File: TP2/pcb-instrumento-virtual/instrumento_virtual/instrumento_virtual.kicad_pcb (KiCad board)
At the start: 2 copper layers, 90 parts, among them J1 Conn_01x09_Pin, J2 Conector_salidas_analógicas, J3 Conn_01x20_Socket, J4 Conn_01x09_Pin, J5 Conn_01x20_Socket, J7 RS232, Q10 BC547, Q3 BC547, Q4 BC547, Q5 BC547, Q6 BC547, Q7 BC547, Q8 BC547, Q9 BC547, U1 CD4051B, U2 MCP6002-xMC, U4 AMS1117-3.3, U5 AMS1117-5.0, U6 MCP6002-xMC

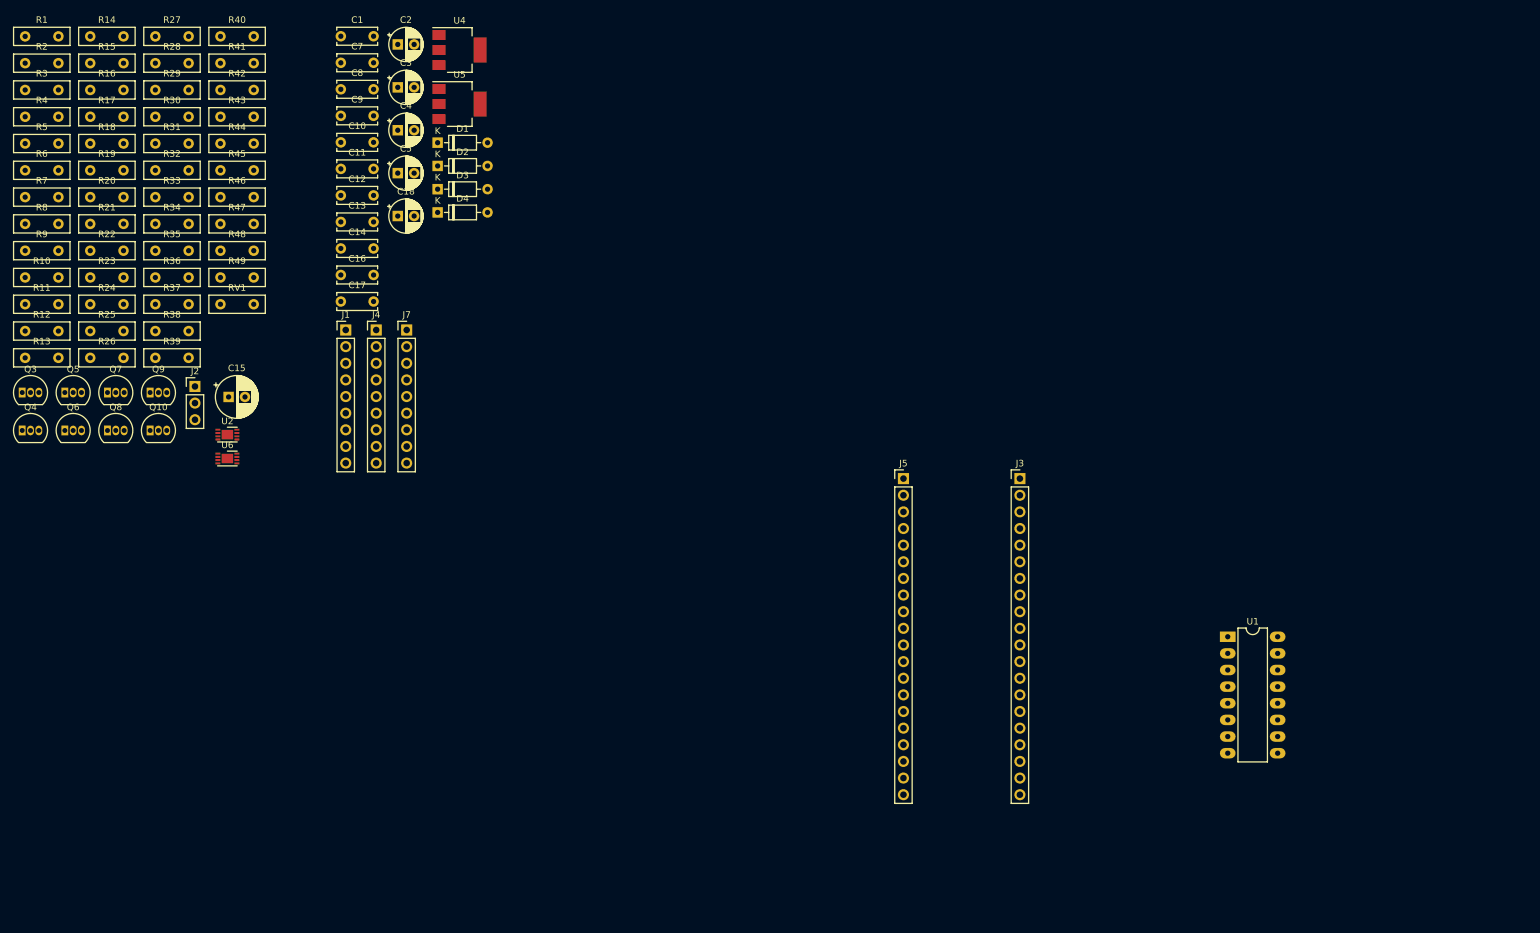
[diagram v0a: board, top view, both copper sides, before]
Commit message: cambiado circuito de adaptacion de niveles logicos
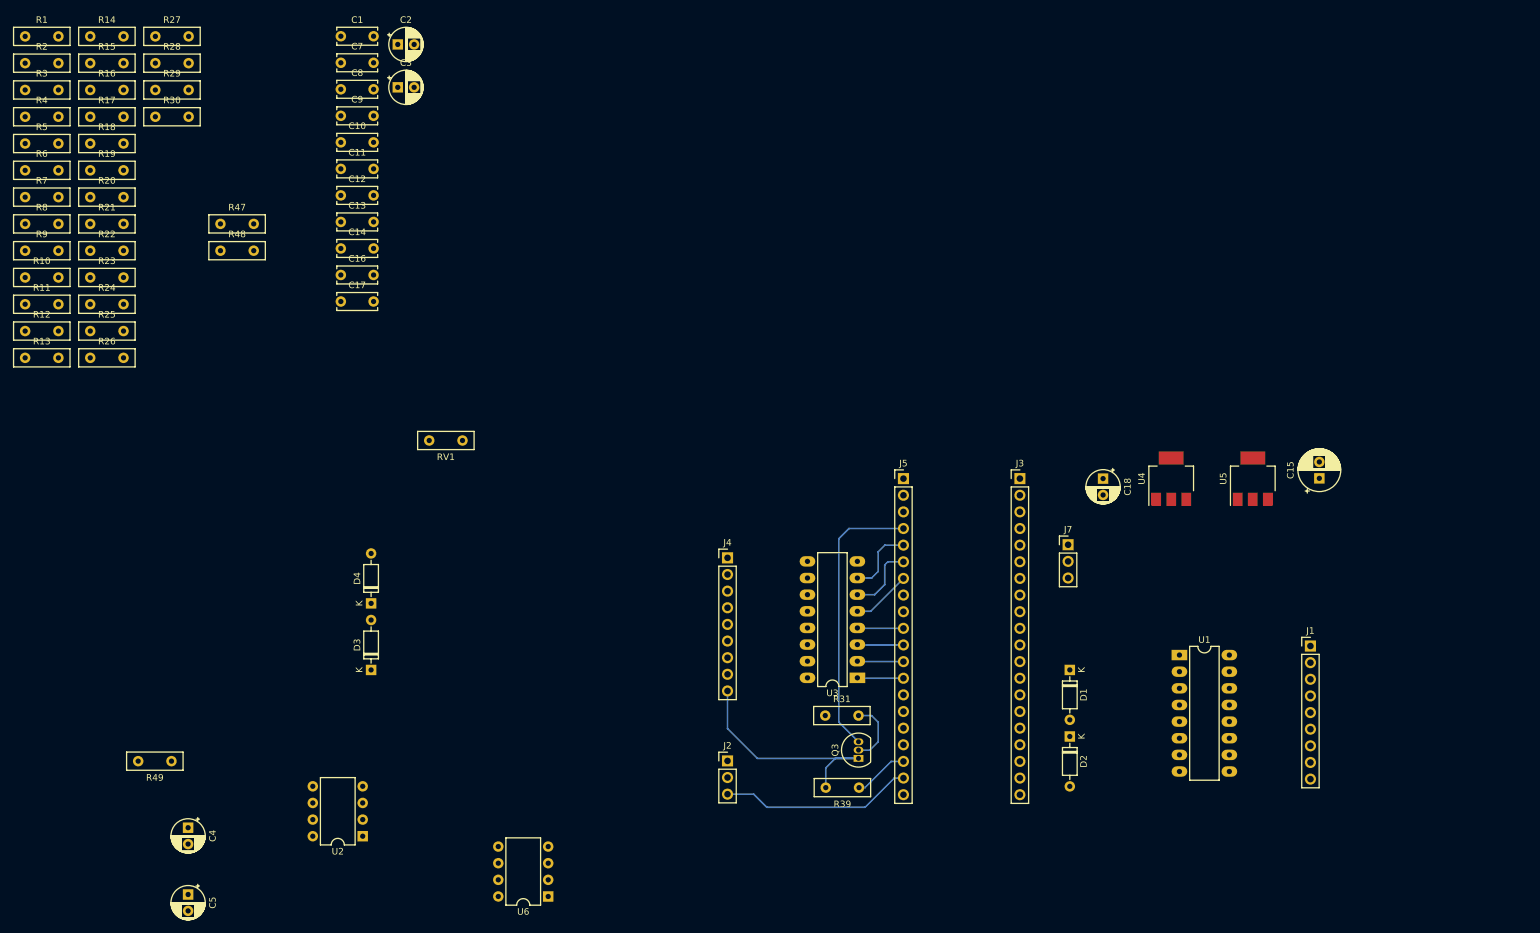
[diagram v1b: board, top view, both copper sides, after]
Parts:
- removed Q10, Q4, Q5, Q6, Q7, Q8, Q9: BC547, Package_TO_SOT_THT:TO-92_Inline
- removed R32, R33, R35, R36, R37, R43, R45: 2.2k, Resistor_THT:R_Box_L8.4mm_W2.5mm_P5.08mm
- removed R34, R38, R40, R41, R42, R44, R46: 6.8k, Resistor_THT:R_Box_L8.4mm_W2.5mm_P5.08mm
- added U3: ULN2003, Package_DIP:DIP-16_W7.62mm_LongPads, F.Cu at (142.8, 114.2)
- J7: footprint Connector_PinHeader_2.54mm:PinHeader_1x09_P2.54mm_Vertical -> Connector_PinHeader_2.54mm:PinHeader_1x03_P2.54mm_Vertical
- U2, U6: footprint Package_DFN_QFN:DFN-8-1EP_3x2mm_P0.5mm_EP1.75x1.45mm -> Package_DIP:DIP-8_W7.62mm
- moved C15 167.0 mm to (213.4, 83.8), turned to 90 degrees
- moved J1 155.0 mm to (212.0, 109.4)
- moved Q3 139.4 mm to (143.0, 126.5), turned to 90 degrees
- moved R31 134.5 mm to (137.9, 120.0)
- moved U5 133.9 mm to (203.2, 83.8), turned to 90 degrees
- moved D2 130.0 mm to (175.3, 123.2), turned to -90 degrees
- moved U4 126.8 mm to (190.7, 83.8), turned to 90 degrees
- moved R39 125.9 mm to (143.1, 131.0), turned to 180 degrees
- moved D1 125.7 mm to (175.3, 113.0), turned to -90 degrees
- moved C18 114.9 mm to (180.3, 83.8), turned to -90 degrees
- moved C5 114.7 mm to (40.6, 147.3), turned to -90 degrees
- moved C4 111.2 mm to (40.6, 137.1), turned to -90 degrees
- moved J7 106.2 mm to (175.0, 93.9)
- moved J2 99.4 mm to (123.0, 126.9)
- moved U6 82.9 mm to (95.6, 147.6), turned to 180 degrees
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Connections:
- J4 pad 3: DOUT7 -> DOUT2
- J4 pad 4: DOUT6 -> DOUT3
- J4 pad 5: DOUT5 -> DOUT4
- J4 pad 6: DOUT4 -> DOUT5
- J4 pad 7: DOUT3 -> DOUT6
- J4 pad 8: DOUT2 -> DOUT7
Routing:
- net PB15: track 0.00 -> 42.7 mm
- net DOUT1: track 0.00 -> 36.2 mm
- net GND: track 0.00 -> 29.5 mm
- net PA9: track 0.00 -> 10.9 mm
- net PA8: track 0.00 -> 10.9 mm
- net Net-(Q3-B): track 0.00 -> 9.94 mm
- net PA10: track 0.00 -> 9.11 mm
- net 5V: track 0.00 -> 8.44 mm
- net PB5: track 0.00 -> 7.06 mm
- net PB4: track 0.00 -> 7.06 mm
- net PB3: track 0.00 -> 7.06 mm
- net PA15: track 0.00 -> 7.06 mm

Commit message: pcb actualizada
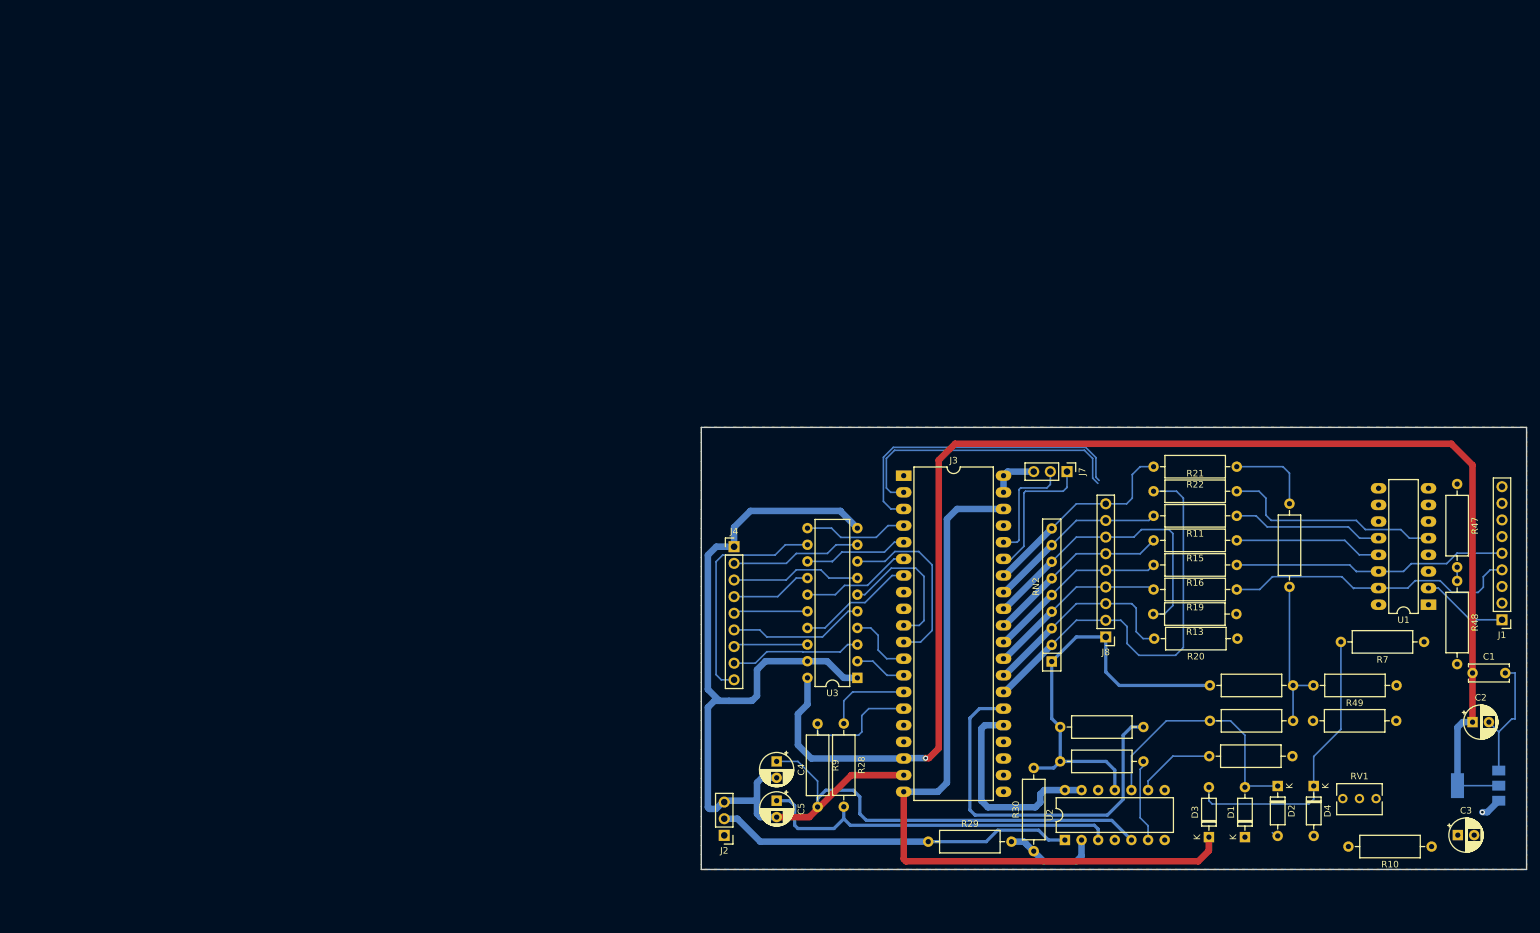
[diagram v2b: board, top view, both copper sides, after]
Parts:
- removed C10, C11, C12, C13, C14, C16, C17, C7, C8, C9: 100n, Capacitor_THT:C_Disc_D6.0mm_W2.5mm_P5.00mm
- removed C15: 100u, Capacitor_THT:CP_Radial_D6.3mm_P2.50mm
- removed C18: 10u, Capacitor_THT:CP_Radial_D5.0mm_P2.50mm
- removed J5: Conn_01x20_Socket, Connector_PinHeader_2.54mm:PinHeader_1x20_P2.54mm_Vertical
- removed Q3: BC547, Package_TO_SOT_THT:TO-92_Inline
- removed R12, R14, R17, R18, R23, R24, R25, R26: 22K, Resistor_THT:R_Box_L8.4mm_W2.5mm_P5.08mm
- removed R31: 2.2k, Resistor_THT:R_Box_L8.4mm_W2.5mm_P5.08mm
- removed R39: 6.8k, Resistor_THT:R_Box_L8.4mm_W2.5mm_P5.08mm
- removed R8: 33k, Resistor_THT:R_Box_L8.4mm_W2.5mm_P5.08mm
- removed U4: AMS1117-3.3, Package_TO_SOT_SMD:SOT-223-3_TabPin2
- removed U6: MCP6002-xMC, Package_DIP:DIP-8_W7.62mm
- added J8: C_Network08, Connector_PinHeader_2.54mm:PinHeader_1x09_P2.54mm_Vertical, F.Cu at (180.8, 108.0)
- added RN2: R_Network08, Resistor_THT:R_Array_SIP9, F.Cu at (172.5, 111.8)
- J1: value Conn_01x09_Pin -> Entradas analógicas
- J3: value Conn_01x20_Socket -> Conn_02x20_Counter_Clockwise_MountingPin; footprint Connector_PinHeader_2.54mm:PinHeader_1x20_P2.54mm_Vertical -> Package_DIP:DIP-40_W15.24mm_LongPads
- R1: value 1M -> 22k; footprint Resistor_THT:R_Box_L8.4mm_W2.5mm_P5.08mm -> Resistor_THT:R_Axial_DIN0309_L9.0mm_D3.2mm_P12.70mm_Horizontal
- R10, R11, R13, R15, R16, R19, R20, R21, R22, R27, R28, R29, R30, R47, R48, R49, R6, R7, R9: footprint Resistor_THT:R_Box_L8.4mm_W2.5mm_P5.08mm -> Resistor_THT:R_Axial_DIN0309_L9.0mm_D3.2mm_P12.70mm_Horizontal
- R2: value 1M -> 22K; footprint Resistor_THT:R_Box_L8.4mm_W2.5mm_P5.08mm -> Resistor_THT:R_Axial_DIN0309_L9.0mm_D3.2mm_P12.70mm_Horizontal
- R3: value 1M -> 33K; footprint Resistor_THT:R_Box_L8.4mm_W2.5mm_P5.08mm -> Resistor_THT:R_Axial_DIN0309_L9.0mm_D3.2mm_P12.70mm_Horizontal
- R4: value 1M -> 32k; footprint Resistor_THT:R_Box_L8.4mm_W2.5mm_P5.08mm -> Resistor_THT:R_Axial_DIN0309_L9.0mm_D3.2mm_P12.70mm_Horizontal
- R5: value 68k -> 100K; footprint Resistor_THT:R_Box_L8.4mm_W2.5mm_P5.08mm -> Resistor_THT:R_Axial_DIN0309_L9.0mm_D3.2mm_P12.70mm_Horizontal
- RV1: footprint Resistor_THT:R_Box_L8.4mm_W2.5mm_P5.08mm -> Potentiometer_THT:Potentiometer_Bourns_3266Y_Vertical
- U2: value MCP6002-xMC -> LM324; footprint Package_DIP:DIP-8_W7.62mm -> Package_DIP:DIP-14_W7.62mm
- U3: value ULN2003 -> 74HC244; footprint Package_DIP:DIP-16_W7.62mm_LongPads -> Package_DIP:DIP-20_W7.62mm
- U5: moved to B.Cu
- moved R1 231.7 mm to (225.2, 115.4), turned to 180 degrees
- moved R10 231.7 mm to (230.5, 140.0), turned to 180 degrees
- moved R7 224.1 mm to (229.3, 108.8), turned to 180 degrees
- moved R2 215.6 mm to (209.3, 115.4), turned to 180 degrees
- moved R6 211.0 mm to (209.3, 120.8), turned to 180 degrees
- moved R4 205.5 mm to (196.6, 126.2)
- moved R3 203.1 mm to (208.8, 87.7), turned to -90 degrees
- moved C1 198.3 mm to (236.8, 113.5)
- moved C3 198.1 mm to (234.5, 138.2)
- moved R48 195.4 mm to (234.4, 99.5), turned to -90 degrees
- moved C2 194.0 mm to (236.8, 121.0)
- moved R47 193.0 mm to (234.4, 84.7), turned to -90 degrees
- moved R5 192.6 mm to (186.5, 121.8), turned to 180 degrees
- moved R15 189.6 mm to (200.8, 93.2), turned to 180 degrees
- moved R16 189.5 mm to (200.8, 97.0), turned to 180 degrees
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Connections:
- C4 pad 1: Net-(U6A-+) -> Net-(U2B-+)
- C4 pad 2: GND -> Net-(U2B-+)
- C5 pad 1: Net-(U6B-+) -> Net-(U2A-+)
- C5 pad 2: GND -> Net-(U2B-+)
- D1 pad 2: PA0 -> Net-(D1-A)
- D2 pad 1: PA0 -> Net-(D1-A)
- J1 pad 1: IN01 -> IN06
- J1 pad 3: IN03 -> IN01
- J1 pad 4: IN04 -> IN05
- J1 pad 5: IN05 -> IN04
- J1 pad 6: IN06 -> IN03
- J2 pad 3: GND -> Net-(U2B-+)
- J3 pad 1: GND -> PB12
- J3 pad 10: PA6 -> PA15
- J3 pad 11: PA5 -> PB3
- J3 pad 12: PA4 -> PB4
- J3 pad 13: PA3 -> PB5
- J3 pad 14: PA2 -> PB6
- J3 pad 15: PA1 -> PB7
- J3 pad 16: PA0 -> PB8
- J3 pad 17: PC15 -> PB9
- J3 pad 18: PC14 -> 5V
- J3 pad 19: PC13 -> Net-(U2B-+)
- J3 pad 2: GND -> PB13
- J3 pad 20: VBAT -> 3V3
- J3 pad 3: 3V3 -> PB14
- J3 pad 4: RST_BUTTON -> PB15
- J3 pad 5: PB11 -> PA8
- J3 pad 6: PB10 -> PA9
- J3 pad 7: PB1 -> PA10
- J3 pad 8: PB0 -> PA11
- J3 pad 9: PA7 -> PA12
- J4 pad 1: GND -> Net-(U2B-+)
- J4 pad 2: DOUT8 -> DOUT1
- J4 pad 6: DOUT5 -> DOUT6
- J4 pad 7: DOUT6 -> DOUT5
- J4 pad 9: DOUT1 -> DOUT8
- J7 pad 1: PB11 -> PB10
- J7 pad 2: PB10 -> PB11
- R1 pad 1: Net-(U2A--) -> OFFSET
- R10 pad 2: Net-(U6A--) -> Net-(U2B--)
- R11 pad 2: PB1 -> C01
- R13 pad 2: PB0 -> C02
- R15 pad 2: PA7 -> C03
- R16 pad 2: PA6 -> C04
- R19 pad 2: PA5 -> C05
- R2 pad 1: Net-(U2A--) -> Net-(R1-Pad2)
- R2 pad 2: Net-(R2-Pad2) -> GND
- R20 pad 2: PA4 -> C06
- R21 pad 1: IN07 -> C07
- R21 pad 2: PA3 -> IN07
- R22 pad 2: PA2 -> C08
- R27 pad 1: Net-(U6A--) -> Net-(U2B--)
- R28 pad 1: PB7 -> PB6
- R28 pad 2: Net-(U6B-+) -> Net-(U2A-+)
- R29 pad 2: Net-(U6B--) -> Net-(U2A--)
- R3 pad 1: OFFSET -> +/-5V
- R3 pad 2: Net-(U2A-+) -> Net-(R1-Pad2)
- R30 pad 1: Net-(U6B--) -> Net-(U2A--)
- R4 pad 1: Net-(U2A-+) -> Net-(U2C--)
- R4 pad 2: GND -> PA0
- R49 pad 1: +3.3V -> 3V3
- R5 pad 1: +/-5V -> PA0
- R5 pad 2: Net-(R2-Pad2) -> GND
- R6 pad 2: PA0 -> Net-(D1-A)
- R9 pad 1: PB6 -> PB7
- R9 pad 2: Net-(U6A-+) -> Net-(U2B-+)
- U1 pad 1: IN05 -> IN02
- U1 pad 11: PB12 -> PB14
- U1 pad 12: IN04 -> IN01
- U1 pad 13: IN01 -> IN03
- U1 pad 14: IN02 -> IN04
- U1 pad 15: IN03 -> IN05
- U1 pad 2: IN07 -> IN06
- U1 pad 5: IN06 -> IN07
- U1 pad 9: PB14 -> PB12
- U2 pad 1: Net-(R1-Pad2) -> AOUT02
- U2 pad 4: GND -> +12V
- U2 pad 5: Net-(D3-A) -> Net-(U2B-+)
- U2 pad 6: PA1 -> Net-(U2B--)
- U2 pad 7: PA1 -> AOUT01
- U2 pad 8: +3.3V -> PA0
- U3 pad 1: PB5 -> Net-(U2B-+)
- U3 pad 10: DOUT2 -> Net-(U2B-+)
- U3 pad 11: DOUT3 -> PB15
- U3 pad 12: DOUT4 -> DOUT8
- U3 pad 13: DOUT5 -> PA8
- U3 pad 14: DOUT6 -> DOUT3
- U3 pad 15: DOUT7 -> PA9
- U3 pad 16: DOUT8 -> DOUT4
- U3 pad 2: PB4 -> PB5
- U3 pad 3: PB3 -> DOUT7
- U3 pad 4: PA15 -> PB4
- U3 pad 5: PA10 -> DOUT6
- U3 pad 6: PA9 -> PA15
- U3 pad 7: PA8 -> DOUT2
- U3 pad 8: GND -> PB3
- U3 pad 9: unconnected-(U3-COM-Pad9) -> DOUT1
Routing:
- net 5V: track 8.44 -> 218.8 mm, vias 0 -> 1
- net Net-(U2B-+): track 0.00 -> 203.3 mm
- net 3V3: track 0.00 -> 116.4 mm
- net C07: track 0.00 -> 64.0 mm
- net GND: track 29.5 -> 91.5 mm
- net PA0: track 0.00 -> 57.9 mm
- net Net-(U2A-+): track 0.00 -> 57.4 mm
- net AOUT02: track 0.00 -> 54.8 mm
- net PB14: track 0.00 -> 47.7 mm
- net IN05: track 0.00 -> 45.7 mm
- net C02: track 0.00 -> 45.7 mm
- net Net-(D3-A): track 0.00 -> 44.3 mm
- net PB13: track 0.00 -> 44.1 mm
- net IN04: track 0.00 -> 42.1 mm
- net Net-(D1-A): track 0.00 -> 38.7 mm
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- added copper zone on B.Cu, net GND
- added copper zone on F.Cu, net GND
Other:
- board outline added: 126 x 67.5 mm

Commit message: version final pcb
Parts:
- removed R49: 10K, Resistor_THT:R_Axial_DIN0309_L9.0mm_D3.2mm_P12.70mm_Horizontal
- added J6: Conn_01x02, Connector_PinSocket_2.54mm:PinSocket_2x01_P2.54mm_Vertical, F.Cu at (242.0, 109.5)
- added R8: 15K, Resistor_THT:R_Axial_DIN0309_L9.0mm_D3.2mm_P12.70mm_Horizontal, F.Cu at (212.4, 120.8)
- added RN1: R_Network08, Resistor_THT:R_Array_SIP9, F.Cu at (142.8, 113.2)
- added U4: TL082, Package_DIP:DIP-8_W7.62mm, F.Cu at (222.8, 125.5)
- C1: footprint Capacitor_THT:C_Disc_D6.0mm_W2.5mm_P5.00mm -> Capacitor_THT:C_Disc_D9.0mm_W2.5mm_P5.00mm
- C2, C4, C5: footprint Capacitor_THT:CP_Radial_D5.0mm_P2.50mm -> Capacitor_THT:CP_Radial_D8.0mm_P5.00mm
- C3: footprint Capacitor_THT:CP_Radial_D5.0mm_P2.50mm -> Capacitor_THT:C_Disc_D9.0mm_W2.5mm_P5.00mm
- moved R10 37.3 mm to (193.4, 135.9), turned to 90 degrees
- moved RV1 8.86 mm to (216.8, 125.5), turned to 90 degrees
- moved U3 6.02 mm to (136.8, 114.4)
- moved C4 4.10 mm to (131.4, 123.0), turned to 180 degrees
- moved C1 2.98 mm to (234.3, 115.2)
- moved C5 2.92 mm to (129.0, 130.5)
- moved J4 1.54 mm to (123.1, 93.0)
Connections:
- C4 pad 2: Net-(U2B-+) -> GND
- C5 pad 2: Net-(U2B-+) -> GND
- J2 pad 3: Net-(U2B-+) -> GND
- J3 pad 19: Net-(U2B-+) -> GND
- J4 pad 1: Net-(U2B-+) -> GND
- RV1 pad 1: OFFSET -> Net-(U4A-+)
- U1 pad 6: unconnected-(U1-INH-Pad6) -> GND
- U3 pad 1: Net-(U2B-+) -> GND
- U3 pad 10: Net-(U2B-+) -> GND
- U3 pad 17: PA10 -> PA15
- U3 pad 19: Net-(U2B-+) -> GND
- U3 pad 6: PA15 -> PA10
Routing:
- net GND: track 91.5 -> 293.7 mm, vias 0 -> 44
- net Net-(U2B-+): track 203.3 -> 66.6 mm
- net +12V: track 3.22 -> 121.4 mm, vias 1 -> 4
- net PB12: track 0.00 -> 80.8 mm
- net AOUT01: track 0.00 -> 76.8 mm, vias 0 -> 2
- net IN02: track 0.00 -> 63.4 mm
- net 3V3: track 116.4 -> 177.6 mm, vias 0 -> 2
- net IN06: track 13.2 -> 62.3 mm
- net +/-5V: track 13.1 -> 57.2 mm
- net IN03: track 22.6 -> 62.6 mm
- net PB13: track 44.1 -> 82.4 mm
- net PA0: track 57.9 -> 95.9 mm
- net PB14: track 47.7 -> 83.7 mm
- net IN07: track 33.8 -> 68.3 mm
- net 5V: track 218.8 -> 249.6 mm, vias 1 -> 2
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- added copper zone on B.Cu, net 5V
- added copper zone on B.Cu, net Net-(U4A-+)
